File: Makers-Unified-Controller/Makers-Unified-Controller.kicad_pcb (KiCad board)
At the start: 2 copper layers, 130.8 x 76.8 mm, 65 parts, among them J1 USB_B_Micro, J2 backup_PROG, Q1 SI2305B-TP, Q2 MMBT3904, Q3 MMBT3904, SW1 SW_DPDT_x2, SW10 SW_Push, SW11 SW_Push, SW12 SW_Push, SW13 SW_Push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

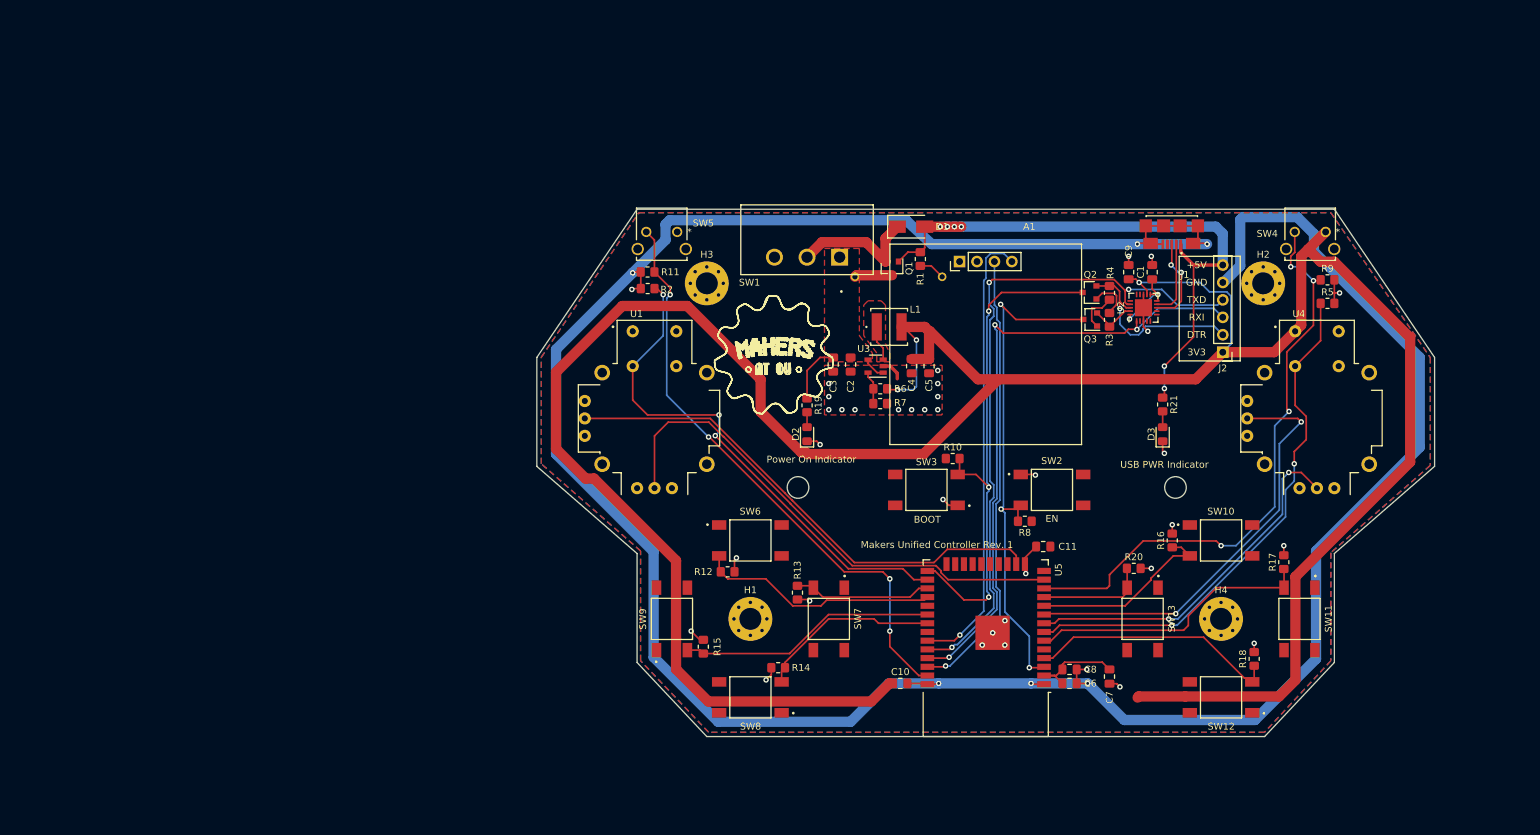
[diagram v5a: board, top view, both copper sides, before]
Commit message: Started PCB - removed unused components from revision 1
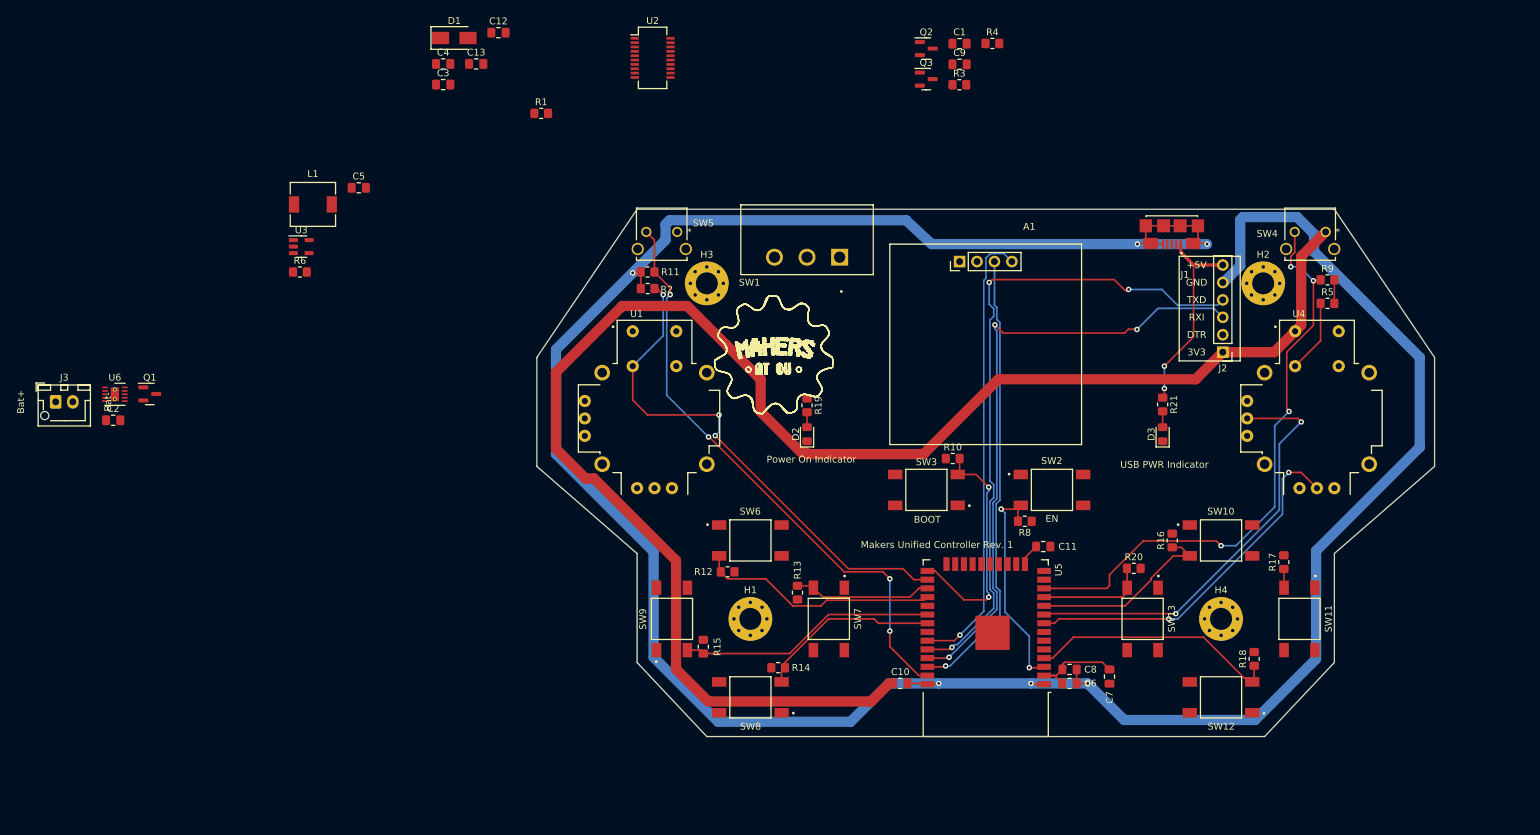
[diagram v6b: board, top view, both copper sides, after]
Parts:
- removed R7: 10k, Resistor_SMD:R_0805_2012Metric_Pad1.20x1.40mm_HandSolder
- added C12: 10u, Capacitor_SMD:C_0805_2012Metric_Pad1.18x1.45mm_HandSolder, F.Cu at (90.3, 26.3)
- added C13: 1u, Capacitor_SMD:C_0805_2012Metric_Pad1.18x1.45mm_HandSolder, F.Cu at (87.0, 30.9)
- added J3: BAT Connector, Footprint_Imports:PRT-18286 Connector, F.Cu at (25.8, 80.1)
- added U6: TPS62046DRCR, Package_SON:VSON-10-1EP_3x3mm_P0.5mm_EP1.2x2mm_ThermalVias, F.Cu at (34.4, 79.0)
- BT1: value BC4AAW -> PRT-18286; footprint Footprint_Imports:BAT_BC4AAW -> Footprint_Imports:PRT18286
- C3, C5: value 1u -> 10u
- C4: value 10u -> 1u
- L1: value 4.7u -> 6.2u; footprint Footprint_Imports:NRS5024T4R7MMGJ -> Inductor_SMD:L_6.3x6.3_H3
- Q1: value SI2305B-TP -> PJA3401A_R1_00001
- R1: value 10k -> 2.2k
- R6: value 47k -> 10k
- U2: value FT231XQ -> FT231XS; footprint Package_DFN_QFN:QFN-20-1EP_4x4mm_P0.5mm_EP2.5x2.5mm -> Package_SO:SSOP-20_3.9x8.7mm_P0.635mm
- U3: value TLV62568DBV -> MCP73832-2-OT
- moved Q1 109.7 mm to (39.5, 79.0), turned to 0 degrees
- moved C2 107.8 mm to (34.2, 82.8), turned to 0 degrees
- moved C5 87.1 mm to (69.9, 48.9), turned to 0 degrees
- moved R6 86.3 mm to (61.4, 61.2), turned to 0 degrees
- moved L1 85.8 mm to (63.3, 51.4)
- moved U3 85.5 mm to (61.6, 57.5), turned to 0 degrees
- moved C4 81.2 mm to (82.2, 30.9), turned to 0 degrees
- moved U2 80.3 mm to (112.8, 30.0), turned to 0 degrees
- moved D1 72.0 mm to (83.9, 27.1)
- moved C3 70.0 mm to (82.2, 33.9), turned to 0 degrees
- moved R1 59.2 mm to (96.5, 38.1), turned to 0 degrees
- moved C1 43.5 mm to (157.5, 27.9), turned to 0 degrees
- moved Q2 42.8 mm to (152.6, 28.7), turned to 0 degrees
- moved Q3 42.4 mm to (152.6, 33.1), turned to 0 degrees
- moved R3 40.6 mm to (157.4, 33.9), turned to 0 degrees
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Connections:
- C4 pad 1: +3V3 -> /PWR_IN
- D3 pad 1: GND -> /CHG_COMPLETE
- J1 pad 4: Net-(J1-Pad4) -> unconnected-(J1-Pad4)
- R1 pad 1: +5V -> Net-(R1-Pad1)
- R6 pad 1: +3V3 -> +5V
- R6 pad 2: Net-(R6-Pad2) -> GND
- U2 pad 1: /BRIDGE_RX -> /BRIDGE_DTR
- U2 pad 10: Net-(C1-Pad1) -> unconnected-(U2-Pad10)
- U2 pad 11: Net-(C1-Pad1) -> /D+
- U2 pad 12: +3V3 -> /D-
- U2 pad 13: GND -> Net-(C1-Pad1)
- U2 pad 14: Net-(U2-Pad14) -> Net-(C1-Pad1)
- U2 pad 15: Net-(U2-Pad15) -> +3V3
- U2 pad 16: Net-(U2-Pad16) -> GND
- U2 pad 17: /BRIDGE_TX -> unconnected-(U2-Pad17)
- U2 pad 18: /BRIDGE_DTR -> unconnected-(U2-Pad18)
- U2 pad 19: /BRIDGE_RTS -> unconnected-(U2-Pad19)
- U2 pad 2: Net-(U2-Pad2) -> /BRIDGE_RTS
- U2 pad 20: Net-(C1-Pad1) -> /BRIDGE_TX
- U2 pad 3: GND -> Net-(C1-Pad1)
- U2 pad 4: Net-(U2-Pad4) -> /BRIDGE_RX
- U2 pad 5: Net-(U2-Pad5) -> unconnected-(U2-Pad5)
- U2 pad 6: Net-(U2-Pad6) -> GND
- U2 pad 7: Net-(U2-Pad7) -> unconnected-(U2-Pad7)
- U2 pad 8: /D+ -> unconnected-(U2-Pad8)
- U2 pad 9: /D- -> unconnected-(U2-Pad9)
- U3 pad 1: /PWR_IN -> /CHG_COMPLETE
- U3 pad 3: Net-(L1-Pad1) -> /BAT+
- U3 pad 4: /PWR_IN -> +5V
- U3 pad 5: Net-(R6-Pad2) -> Net-(R1-Pad1)
- U5 pad 13: /LEFT_JOY_X -> /RIGHT_JOY_SW
- U5 pad 14: Net-(U5-Pad14) -> unconnected-(U5-Pad14)
- U5 pad 16: /LEFT_JOY_Y -> /SW_6
- U5 pad 17: Net-(U5-Pad17) -> unconnected-(U5-Pad17)
- U5 pad 18: Net-(U5-Pad18) -> unconnected-(U5-Pad18)
- U5 pad 19: Net-(U5-Pad19) -> unconnected-(U5-Pad19)
- U5 pad 20: Net-(U5-Pad20) -> unconnected-(U5-Pad20)
- U5 pad 21: Net-(U5-Pad21) -> unconnected-(U5-Pad21)
- U5 pad 22: Net-(U5-Pad22) -> unconnected-(U5-Pad22)
- U5 pad 23: Net-(U5-Pad23) -> unconnected-(U5-Pad23)
- U5 pad 24: Net-(U5-Pad24) -> unconnected-(U5-Pad24)
- U5 pad 29: Net-(U5-Pad29) -> unconnected-(U5-Pad29)
- U5 pad 32: Net-(U5-Pad32) -> unconnected-(U5-Pad32)
- U5 pad 5: Net-(U5-Pad5) -> unconnected-(U5-Pad5)
- U5 pad 6: /SW_6 -> /LEFT_JOY_Y
- U5 pad 7: /RIGHT_JOY_SW -> /LEFT_JOY_X
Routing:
- net +3V3: track 412.9 -> 246.9 mm, vias 3 -> 0
- net /LEFT_JOY_X: track 74.9 -> 0.00 mm
- net /LEFT_JOY_Y: track 74.0 -> 0.00 mm
- net /RIGHT_JOY_SW: track 76.7 -> 10.7 mm, vias 2 -> 0
- net +5V: track 88.5 -> 29.3 mm, vias 6 -> 2
- net GND: track 445.9 -> 401.2 mm, vias 42 -> 6
- net /EN: track 75.8 -> 32.6 mm, vias 3 -> 2
- net /IO0: track 76.1 -> 34.8 mm, vias 3 -> 2
- net /SW_6: track 41.7 -> 2.74 mm
- net /BRIDGE_DTR: track 27.3 -> 0.00 mm, vias 1 -> 0
- net Net-(D1-Pad1): track 19.3 -> 0.00 mm
- net /D+: track 13.2 -> 0.00 mm, vias 2 -> 0
- net /PWR_IN: track 12.0 -> 0.00 mm
- net /D-: track 11.2 -> 0.00 mm
- net Net-(C1-Pad1): track 10.8 -> 0.00 mm, vias 2 -> 0
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- removed copper zone on F.Cu, net +3V3
- removed copper zone on F.Cu, net /PWR_IN
- removed copper zone on B.Cu, net GND
- removed copper zone on F.Cu, net GND
- removed copper zone on F.Cu, net Net-(L1-Pad1)
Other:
- net class Default removed

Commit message: Completed routing - TODO final checks
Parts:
- J3: moved to B.Cu
- moved J3 128.8 mm to (153.7, 64.8), turned to 180 degrees
- moved Q1 112.0 mm to (149.9, 59.7), turned to -90 degrees
- moved C2 111.2 mm to (144.8, 71.1)
- moved U6 107.4 mm to (141.7, 80.4), turned to -90 degrees
- moved U3 100.0 mm to (161.3, 64.8), turned to 90 degrees
- moved R6 92.3 mm to (153.7, 60.0), turned to -90 degrees
- moved L1 85.8 mm to (141.0, 87.6), turned to -90 degrees
- moved C13 84.4 mm to (143.5, 93.6), turned to -90 degrees
- moved C12 84.2 mm to (141.0, 93.6), turned to -90 degrees
- moved C5 81.8 mm to (138.4, 93.6), turned to -90 degrees
- moved C4 77.2 mm to (144.8, 76.2)
- moved U2 77.1 mm to (181.6, 64.8), turned to 90 degrees
- moved C3 74.1 mm to (144.8, 73.7)
- moved D1 73.7 mm to (151.7, 55.9)
- moved R1 67.2 mm to (158.1, 65.0), turned to -90 degrees
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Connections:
- net Net-(L1-Pad1) renamed /Power Management/BUCK_SW
- SW1 pad 3: Net-(SW1-Pad3) -> unconnected-(SW1-Pad3)
- U6 pad 11: (no net) -> GND
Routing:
- net /LEFT_JOY_Y: track 0.00 -> 98.1 mm, vias 0 -> 2
- net /LEFT_JOY_X: track 0.00 -> 92.2 mm, vias 0 -> 4
- net +3V3: track 246.9 -> 321.9 mm, vias 0 -> 1
- net +5V: track 29.3 -> 92.6 mm, vias 2 -> 5
- net /RIGHT_JOY_SW: track 10.7 -> 72.1 mm
- net GND: track 401.2 -> 451.7 mm, vias 6 -> 36
- net /SW_6: track 2.74 -> 52.0 mm, vias 0 -> 2
- net /CHG_COMPLETE: track 0.00 -> 47.0 mm, vias 0 -> 2
- net /EN: track 32.6 -> 66.3 mm, vias 2 -> 3
- net /BRIDGE_DTR: track 0.00 -> 29.0 mm, vias 0 -> 1
- net /IO0: track 34.8 -> 61.6 mm, vias 2 -> 3
- net /BAT+: track 0.00 -> 19.3 mm
- net Net-(D1-Pad1): track 0.00 -> 18.9 mm
- net /PWR_IN: track 0.00 -> 13.6 mm
- net /BRIDGE_RTS: track 0.00 -> 12.6 mm, vias 0 -> 2
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- added copper zone on F.Cu, net +3V3
- added copper zone on F.Cu, net /PWR_IN
- added copper zone on F.Cu, net /Power Management/BUCK_SW
- added copper zone on B.Cu, net GND

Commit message: Finalized layout and exported files
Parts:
- moved BT1 17.0 mm to (150.8, 108.8)
- moved C11 17.0 mm to (157.9, 113.5)
- moved C3 17.0 mm to (133.1, 85.9)
- moved C7 17.0 mm to (167.6, 132.4)
- moved C8 17.0 mm to (161.8, 131.4)
- moved D3 17.0 mm to (175.3, 97.1)
- moved J2 17.0 mm to (184.1, 85.2)
- moved L1 17.0 mm to (129.2, 99.9)
- moved Q1 17.0 mm to (138.1, 72.0)
- moved R13 17.0 mm to (122.1, 120.2)
- moved R3 17.0 mm to (165.3, 91.0)
- moved R9 17.0 mm to (199.4, 74.6)
- moved SW10 17.0 mm to (183.9, 112.6)
- moved SW12 17.0 mm to (183.9, 135.5)
- moved SW2 17.0 mm to (159.2, 105.2)
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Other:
- board text added: "Charging Indicator"
- board text added: "Designers: Revision 1 & 2 - Matthew Bellafaire (2021)"
- board text added: "Makers Unified Controller Rev. 2"
- board text removed: "Makers Unified Controller Rev. 1"
- board text removed: "USB PWR Indicator"
